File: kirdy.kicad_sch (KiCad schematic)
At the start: 0 parts

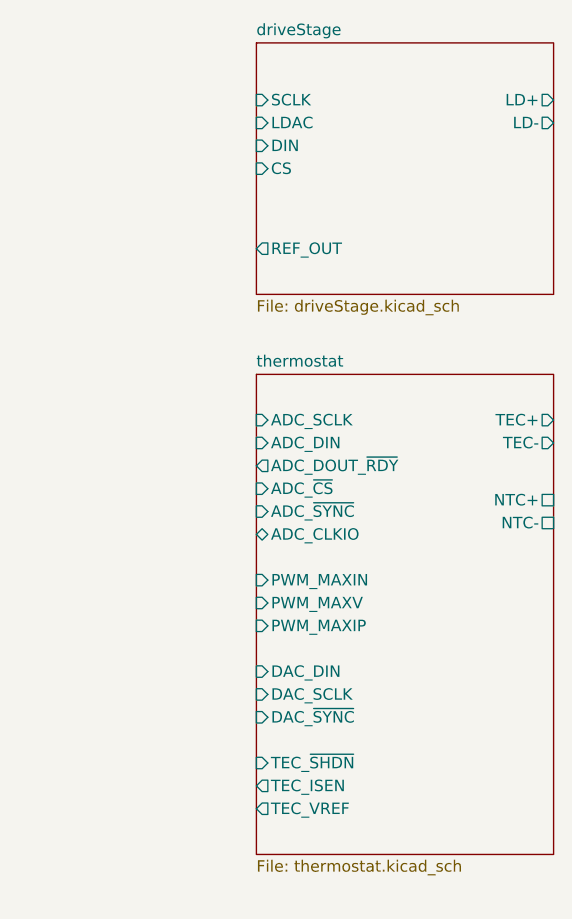
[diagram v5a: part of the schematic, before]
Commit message: add TEC V sense, filter TEC I sense
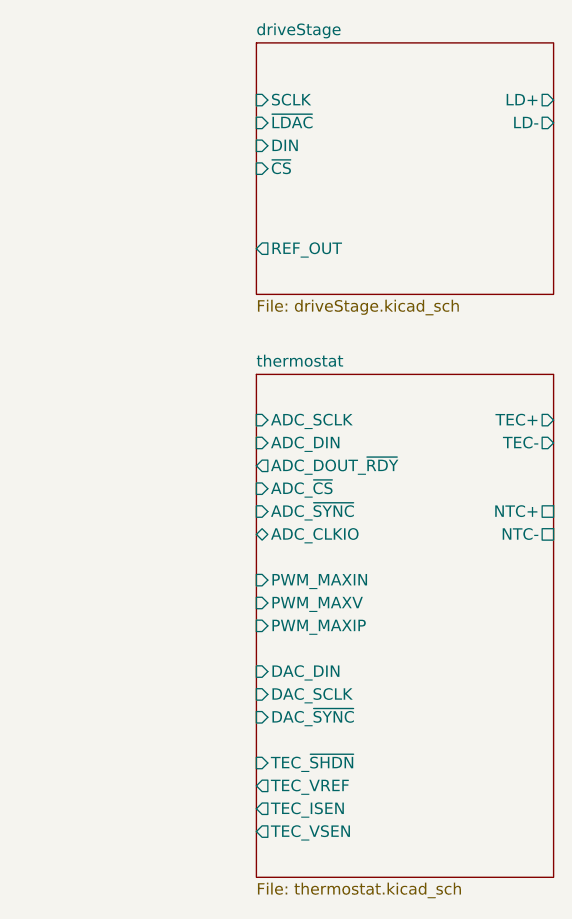
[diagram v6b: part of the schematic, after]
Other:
- sheet driveStage ports: added ~{CS}, ~{LDAC}; removed CS, LDAC
- sheet thermostat ports: added TEC_VSEN; removed none
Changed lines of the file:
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@@
-      (effects (font (size 1.27 1.27)) (justify left))
-    )
-    (pin "LDAC" input (at 262.89 102.87 180)
       (effects (font (size 1.27 1.27)) (justify left))
     )
@@
       (effects (font (size 1.27 1.27)) (justify left))
     )
-    (pin "CS" input (at 262.89 107.95 180)
+    (pin "~{LDAC}" input (at 262.89 102.87 180)
+      (effects (font (size 1.27 1.27)) (justify left))
+    )
+    (pin "~{CS}" input (at 262.89 107.95 180)
       (effects (font (size 1.27 1.27)) (justify left))
     )
   )
-  (sheet (at 262.89 130.81) (size 33.02 53.34) (fields_autoplaced)
+  (sheet (at 262.89 130.81) (size 33.02 55.88) (fields_autoplaced)
     (stroke (width 0.1524) (type solid) (color 0 0 0 0))
     (fill (color 0 0 0 0.0000))
@@
       (effects (font (size 1.27 1.27)) (justify left bottom))
     )
-    (property "Sheet file" "thermostat.kicad_sch" (id 1) (at 262.89 184.7346 0)
+    (property "Sheet file" "thermostat.kicad_sch" (id 1) (at 262.89 187.2746 0)
       (effects (font (size 1.27 1.27)) (justify left top))
     )
@@
       (effects (font (size 1.27 1.27)) (justify right))
     )
-    (pin "NTC-" passive (at 295.91 147.32 0)
+    (pin "NTC-" passive (at 295.91 148.59 0)
       (effects (font (size 1.27 1.27)) (justify right))
     )
-    (pin "NTC+" passive (at 295.91 144.78 0)
+    (pin "NTC+" passive (at 295.91 146.05 0)
       (effects (font (size 1.27 1.27)) (justify right))
     )
@@
       (effects (font (size 1.27 1.27)) (justify left))
     )
-    (pin "TEC_ISEN" output (at 262.89 176.53 180)
-      (effects (font (size 1.27 1.27)) (justify left))
-    )
-    (pin "TEC_VREF" output (at 262.89 179.07 180)
+    (pin "TEC_ISEN" output (at 262.89 179.07 180)
+      (effects (font (size 1.27 1.27)) (justify left))
+    )
+    (pin "TEC_VREF" output (at 262.89 176.53 180)
+      (effects (font (size 1.27 1.27)) (justify left))
+    )
+    (pin "TEC_VSEN" output (at 262.89 181.61 180)
       (effects (font (size 1.27 1.27)) (justify left))
     )
@@
       (reference "#PWR?") (unit 1) (value "GND") (footprint "")
     )
+    (path "/bda728c0-b189-4e05-8d4f-58a38acf883b/2c5144e0-6676-488a-8854-2644e10311f8"
+      (reference "#PWR?") (unit 1) (value "GND") (footprint "")
+    )
     (path "/7fc2620b-bac4-49c0-a276-7d2a46898037/30c37857-bcd7-4d18-b782-dd4e651118cd"
       (reference "#PWR?") (unit 1) (value "-6V") (footprint "")
@@
       (reference "#PWR?") (unit 1) (value "GND") (footprint "")
     )
+    (path "/bda728c0-b189-4e05-8d4f-58a38acf883b/7c3a7fd2-8a01-4018-8431-715b54a03df5"
+      (reference "#PWR?") (unit 1) (value "GND") (footprint "")
+    )
     (path "/7fc2620b-bac4-49c0-a276-7d2a46898037/7f2ae8de-9741-4de8-8b3e-0cbf1d496d0b"
       (reference "#PWR?") (unit 1) (value "GND") (footprint "")
@@
       (reference "#PWR?") (unit 1) (value "GND") (footprint "")
     )
+    (path "/bda728c0-b189-4e05-8d4f-58a38acf883b/92b3fabc-a06c-46bf-b3bc-8ea6e9e7a24a"
+      (reference "#PWR?") (unit 1) (value "GND") (footprint "")
+    )
     (path "/7fc2620b-bac4-49c0-a276-7d2a46898037/94d8c0ef-788e-401d-b84d-b1e1c20b5ad0"
       (reference "#PWR?") (unit 1) (value "+15V") (footprint "")
@@
       (reference "#PWR?") (unit 1) (value "GND") (footprint "")
     )
+    (path "/bda728c0-b189-4e05-8d4f-58a38acf883b/f06b748e-f289-4f69-90c4-f4518cf53962"
+      (reference "#PWR?") (unit 1) (value "GND") (footprint "")
+    )
     (path "/7fc2620b-bac4-49c0-a276-7d2a46898037/f4f71da4-602f-4bb4-aa0d-484f08abc473"
       (reference "#PWR?") (unit 1) (value "+15V") (footprint "")
@@
       (reference "C?") (unit 1) (value "10u") (footprint "")
     )
+    (path "/bda728c0-b189-4e05-8d4f-58a38acf883b/39a9cf43-5ef2-4a90-be44-7904dfcca88e"
+      (reference "C?") (unit 1) (value "100n") (footprint "")
+    )
     (path "/7fc2620b-bac4-49c0-a276-7d2a46898037/3a9b3bec-ffe0-47c1-b9ff-bb9db7bc2b51"
       (reference "C?") (unit 1) (value "10u") (footprint "")
@@
       (reference "C?") (unit 1) (value "100n") (footprint "")
     )
+    (path "/bda728c0-b189-4e05-8d4f-58a38acf883b/81b74c6f-70d9-47ec-b9c4-05f58580a6c2"
+      (reference "C?") (unit 1) (value "100n") (footprint "")
+    )
     (path "/bda728c0-b189-4e05-8d4f-58a38acf883b/82083421-60e5-4965-a439-ddc423605cc4"
       (reference "C?") (unit 1) (value "100n") (footprint "")
@@
       (reference "C?") (unit 1) (value "10n") (footprint "")
     )
+    (path "/bda728c0-b189-4e05-8d4f-58a38acf883b/e25c619e-476b-4774-9b03-a1b8a847afae"
+      (reference "C?") (unit 1) (value "10u") (footprint "")
+    )
     (path "/7fc2620b-bac4-49c0-a276-7d2a46898037/e2977f65-f85a-4c87-95bf-ecd689fc10da"
       (reference "C?") (unit 1) (value "100n") (footprint "")
@@
       (reference "D?") (unit 1) (value "AQ4020-01FTG-C") (footprint "")
     )
+    (path "/bda728c0-b189-4e05-8d4f-58a38acf883b/b31815cc-6d80-43d7-aa80-8f2cba5ff682"
+      (reference "FL?") (unit 1) (value "5A") (footprint "")
+    )
     (path "/7fc2620b-bac4-49c0-a276-7d2a46898037/fc3e1e88-39dd-4e44-9550-0de98037638f"
       (reference "J?") (unit 1) (value "MOD_IN") (footprint "")
@@
       (reference "R?") (unit 1) (value "33") (footprint "")
     )
+    (path "/bda728c0-b189-4e05-8d4f-58a38acf883b/1fa4775d-2f38-404f-a520-31db869a64ed"
+      (reference "R?") (unit 1) (value "10k") (footprint "")
+    )
     (path "/bda728c0-b189-4e05-8d4f-58a38acf883b/221bde9e-cb59-4ff6-9f67-7d59ab678667"
       (reference "R?") (unit 1) (value "10k") (footprint "")
@@
       (reference "R?") (unit 1) (value "100") (footprint "")
     )
+    (path "/bda728c0-b189-4e05-8d4f-58a38acf883b/44a2395e-312c-4d6f-a55b-0231227a188b"
+      (reference "R?") (unit 1) (value "1k6") (footprint "")
+    )
     (path "/bda728c0-b189-4e05-8d4f-58a38acf883b/45db473a-56b4-4b6e-b3ce-f172faf6ebfb"
       (reference "R?") (unit 1) (value "10k") (footprint "")
@@
       (reference "R?") (unit 1) (value "5k11 5ppm") (footprint "")
     )
+    (path "/bda728c0-b189-4e05-8d4f-58a38acf883b/8473260b-f8b5-4318-a7c1-697507f18108"
+      (reference "R?") (unit 1) (value "20k") (footprint "")
+    )
     (path "/7fc2620b-bac4-49c0-a276-7d2a46898037/84d1caf1-6f0d-4adb-bda1-ca435ebeff03"
       (reference "R?") (unit 1) (value "2k") (footprint "")
@@
       (reference "R?") (unit 1) (value "33") (footprint "")
     )
+    (path "/bda728c0-b189-4e05-8d4f-58a38acf883b/a4418b7a-65be-4356-ab11-4a0fa489dbf8"
+      (reference "R?") (unit 1) (value "10k") (footprint "")
+    )
     (path "/7fc2620b-bac4-49c0-a276-7d2a46898037/affb61ec-84ab-440d-a648-f96126f479ed"
       (reference "R?") (unit 1) (value "100") (footprint "")
@@
       (reference "R?") (unit 1) (value "33") (footprint "")
     )
+    (path "/bda728c0-b189-4e05-8d4f-58a38acf883b/c1e44c79-6482-4029-8aa1-c2cfbba7a9df"
+      (reference "R?") (unit 1) (value "10k") (footprint "")
+    )
     (path "/7fc2620b-bac4-49c0-a276-7d2a46898037/c5994ec4-b59b-4eb4-8847-d4ef36a60a0c"
       (reference "R?") (unit 1) (value "1") (footprint "")
@@
       (reference "R?") (unit 1) (value "10") (footprint "")
     )
+    (path "/bda728c0-b189-4e05-8d4f-58a38acf883b/e357faf5-1e06-4798-810c-fc4d3cc75993"
+      (reference "R?") (unit 1) (value "10k") (footprint "")
+    )
     (path "/bda728c0-b189-4e05-8d4f-58a38acf883b/edda9e7f-324e-4471-a517-82a4a5e6737b"
       (reference "R?") (unit 1) (value "10k") (footprint "")
+    )
+    (path "/bda728c0-b189-4e05-8d4f-58a38acf883b/f4531b53-4ecb-427a-9795-28ef6712f713"
+      (reference "R?") (unit 1) (value "20k") (footprint "")
     )
     (path "/7fc2620b-bac4-49c0-a276-7d2a46898037/6f857960-a9ff-452e-bba2-080502805e7a"
@@
       (reference "U?") (unit 1) (value "MAX1968xUI") (footprint "Package_SO:HTSSOP-28-1EP_4.4x9.7mm_P0.65mm_EP2.85x5.4mm")
     )
+    (path "/bda728c0-b189-4e05-8d4f-58a38acf883b/abf156bf-1d46-408e-ae61-0af00cc5a66e"
+      (reference "U?") (unit 1) (value "RS8552") (footprint "Package_SO:SOIC-8_3.9x4.9mm_P1.27mm")
+    )
     (path "/7fc2620b-bac4-49c0-a276-7d2a46898037/cab8be84-b688-4aaa-b54c-d8be85dc55c5"
       (reference "U?") (unit 1) (value "ADA4898-1YRDZ") (footprint "Package_SO:SOIC-8-1EP_3.9x4.9mm_P1.27mm_EP2.29x3mm")
@@
       (reference "U?") (unit 1) (value "MAX5719xSD") (footprint "Package_SO:SOIC-14_3.9x8.7mm_P1.27mm")
     )
+    (path "/bda728c0-b189-4e05-8d4f-58a38acf883b/f579b708-fd22-4390-9082-6007320c6fd0"
+      (reference "U?") (unit 2) (value "RS8552") (footprint "Package_SO:SOIC-8_3.9x4.9mm_P1.27mm")
+    )
+    (path "/bda728c0-b189-4e05-8d4f-58a38acf883b/28134816-75e2-4d31-b647-7e6e30efddc9"
+      (reference "U?") (unit 3) (value "RS8552") (footprint "Package_SO:SOIC-8_3.9x4.9mm_P1.27mm")
+    )
   )

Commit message: before beer
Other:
- added sheet analog supply (asupply.kicad_sch)
- sheet driveStage ports: added PD_A, PD_BIAS, PD_C, PD_MON; removed none
